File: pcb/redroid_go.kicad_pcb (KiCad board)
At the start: 2 copper layers, 70 x 95 mm, 100 parts, among them J1 USB4105-GF-A, J2 5051101892, J3 Conn_01x02_Pin, J4 Conn_01x10_Pin, Q1 UMH3N, Q2 PMOS, Q3 UMH3N, SW1 UP, SW10 A, SW11 SW_SPDT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

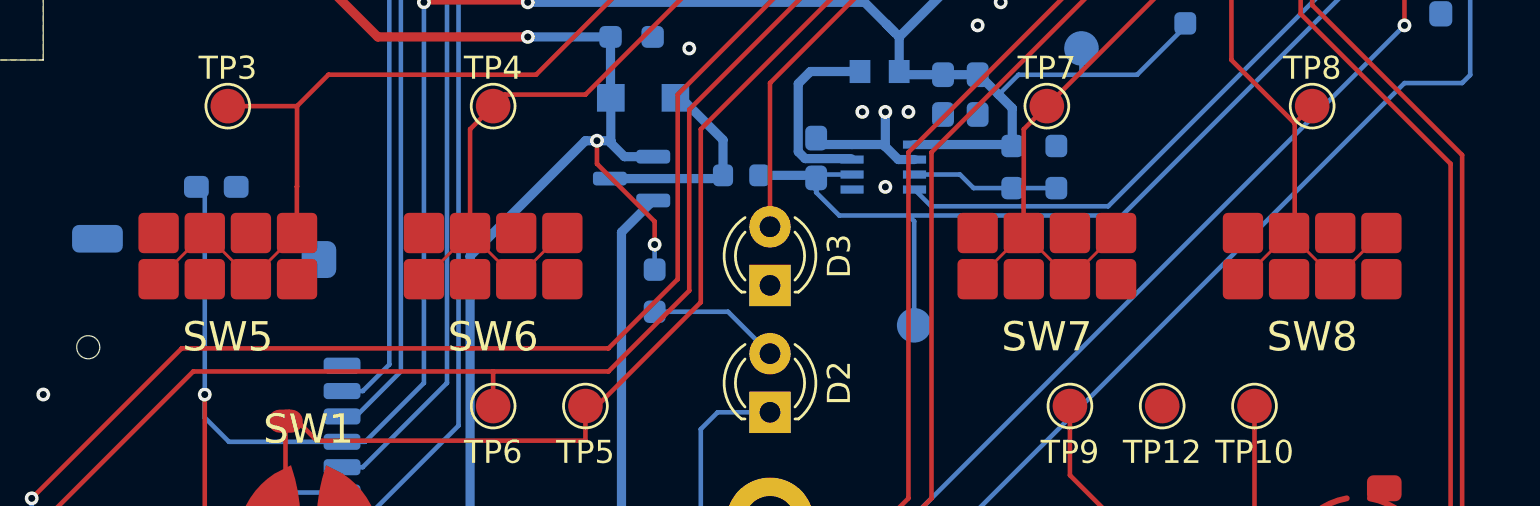
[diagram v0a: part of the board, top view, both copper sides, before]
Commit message: Move menu buttons up
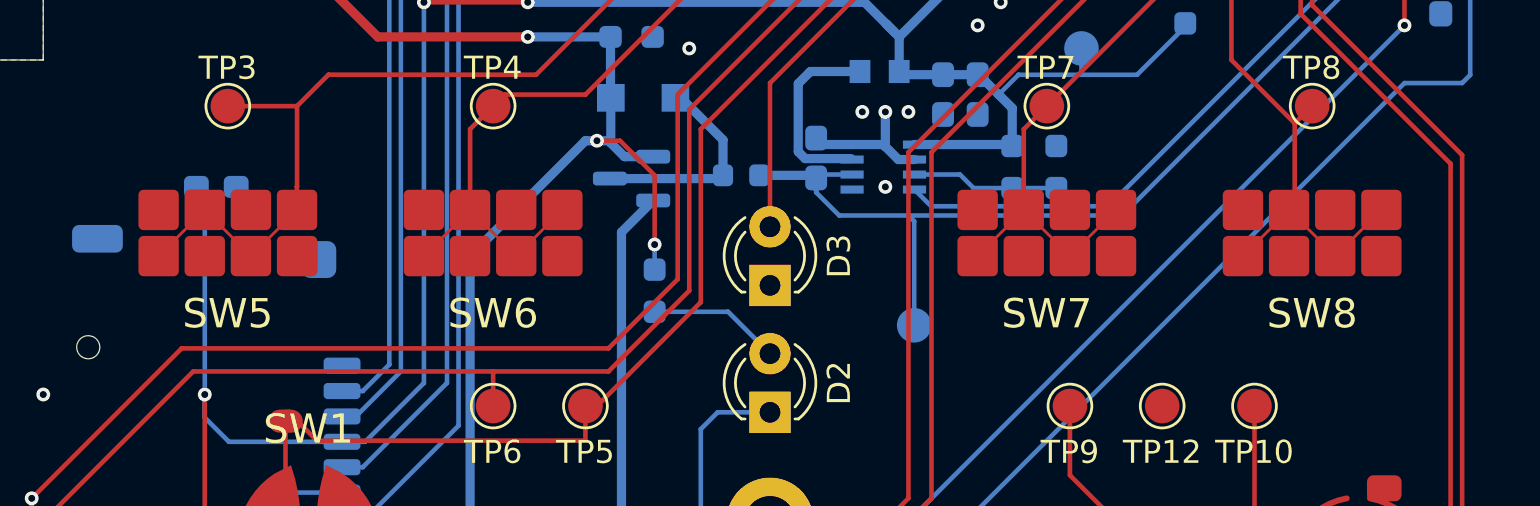
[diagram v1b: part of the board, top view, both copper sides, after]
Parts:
- moved SW5 1.00 mm to (140.0, 103.5)
- moved SW6 1.00 mm to (151.5, 103.5)
- moved SW7 1.00 mm to (175.5, 103.5)
- moved SW8 1.00 mm to (187.0, 103.5)
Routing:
- net IO39: track 55.6 -> 54.9 mm
- net VBUS: track 122.1 -> 122.7 mm
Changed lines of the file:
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@@
 	(footprint "Conductive Button:CONDUCTIVE_BUTTON_THICK_STARTSELECT"
 		(layer "F.Cu")
-		(at 187 104.5)
+		(at 187 103.5)
 		(property "Reference" "SW8"
 			(at 0 3.5 0)
@@
 	(footprint "Conductive Button:CONDUCTIVE_BUTTON_THICK_STARTSELECT"
 		(layer "F.Cu")
-		(at 175.5 104.5)
+		(at 175.5 103.5)
 		(property "Reference" "SW7"
 			(at 0 3.5 0)
@@
 	(footprint "Conductive Button:CONDUCTIVE_BUTTON_THICK_STARTSELECT"
 		(layer "F.Cu")
-		(at 140 104.5)
+		(at 140 103.5)
 		(property "Reference" "SW5"
 			(at 0 3.5 0)
@@
 	(footprint "Conductive Button:CONDUCTIVE_BUTTON_THICK_STARTSELECT"
 		(layer "F.Cu")
-		(at 151.5 104.5)
+		(at 151.5 103.5)
 		(property "Reference" "SW6"
 			(at 0 3.5 0)
@@
 	)
 	(segment
-		(start 158.5 104)
-		(end 158.5 103)
+		(start 158.5 101)
+		(end 157 99.5)
 		(width 0.2)
 		(layer "F.Cu")
@@
 	)
 	(segment
-		(start 158.5 103)
-		(end 156 100.5)
+		(start 157 99.5)
+		(end 156 99.5)
 		(width 0.2)
 		(layer "F.Cu")
@@
 	)
 	(segment
-		(start 156 100.5)
-		(end 156 99.5)
+		(start 136.25 57.62)
+		(end 136.5 57.37)
 		(width 0.2)
 		(layer "F.Cu")
@@
 	)
 	(segment
-		(start 136.25 57.62)
-		(end 136.5 57.37)
+		(start 158.5 104)
+		(end 158.5 101)
 		(width 0.2)
 		(layer "F.Cu")
@@
 		(net 50)
 	)
-	(segment
-		(start 150.5 102.98452)
-		(end 150.24226 103.24226)
-		(width 0.2)
-		(layer "F.Cu")
-		(net 50)
-	)
 	(via
 		(at 173 67)
@@
 	)
 	(segment
-		(start 186.24226 102.74226)
-		(end 185.74226 103.24226)
-		(width 0.2)
-		(layer "F.Cu")
-		(net 59)
-	)
-	(segment
 		(start 182.55 90.45)
 		(end 182.55 71.95)
@@
 	)
 	(segment
-		(start 142.99226 102.99226)
-		(end 142.74226 103.24226)
-		(width 0.2)
-		(layer "F.Cu")
-		(net 61)
-	)
-	(segment
 		(start 153.3625 96.6375)
 		(end 160.5 89.5)
@@
 		(width 0.2)
 		(layer "F.Cu")
-		(net 62)
-	)
-	(segment
-		(start 174.49226 102.99226)
-		(end 174.24226 103.24226)
-		(width 0.2)
-		(layer "F.Cu")
